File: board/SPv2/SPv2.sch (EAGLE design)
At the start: 64 parts, among them IC1 S34ML0XG1, IC2 F55[0/1]X---PT48, IC3 S34ML0XG1, IC4 74LS14D, IC5 F55[0/1]X---PT48, IC6 74LS14D, Q1 12MHz, Q2 12MHz

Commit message: Snap Pad v2, halfsies design, routed
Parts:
- removed C10, C9: 220nF, Passives:C0805
- removed C11, C12: 10pF, Passives:C0805
- removed C13, C15: 20pF, Passives:C0805
- removed C16: 470nF, Passives:C0805
- removed C8: 4.7uF, Passives:C0805
- removed D2: (no value), Passives:D-SCHOTTKY
- removed IC3: S34ML0XG1, Flash:S34ML0XG1
- removed IC5: F55[0/1]X---PT48, TI_MSP430_v16:F55[0/1]X---PT48
- removed IC6: 74LS14D, 74xx-us:74LS14D
- removed JP2: USBPCB, SparkFun-Connectors:USBPCB
- removed Q2: 12MHz, Passives:CRYSTALCSM-3X
- removed R10, R13: 1M, Passives:R0805
- removed R11: 1.4K 1%, Passives:R0805
- removed R12: 100 5%, Passives:R0805
- removed R14, R15: 1.4k, Passives:R0805
- removed R8, R9: 27 5%, Passives:R0805
- removed SJ2: (no value), jumper:SJW
- removed U$12, U$13, U$14, U$3: LED, Passives:LED
- removed U$15, U$16, U$17, U$18: 130, Passives:R0805
- IC2: value F55[0/1]X---PT48 -> F5508
- U$2: value FSMSM -> SNAP-HALF; device Passives:FSMSM -> Passives:SNAP-HALF
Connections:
- removed net !CE!_B: IC3.!CE, IC5.32
- removed net !RE!_B: IC3.!RE, IC5.35
- removed net !RST_B!: IC5.48, R13.1
- removed net !WE!_B: IC3.!WE, IC5.30
- removed net !WP!_B: IC3.!WP, IC5.29
- removed net +1V8_B: C10.1, IC5.43
- removed net +3V3_B: C9.1, IC3.VCC, IC5.11, IC5.28, IC5.42, IC5.7, R12.2, R13.2, U$12.ANODE, U$13.ANODE, U$14.ANODE, U$3.ANODE
- removed net ALE_B: IC3.ALE, IC5.22
- removed net CLE_B: IC3.CLE, IC5.31
- removed net D+_B: C11.1, IC5.38, R10.2, R11.1, R8.1
- removed net D-_B: C12.1, IC5.40, R9.1
- removed net DOUT_B: IC5.1, R14.1, R15.2
- removed net INTER_RXA_TXB: IC2.34, IC5.33
- removed net INTER_RXB_TXA: IC2.33, IC5.34
- removed net N$12: JP2.D+, R8.2
- removed net N$13: JP2.D-, R9.2
- removed net N$14: C16.1, IC5.13
- removed net N$15: U$13.CATHODE, U$17.1
- removed net N$16: U$12.CATHODE, U$16.1
- removed net N$17: U$15.1, U$3.CATHODE
- removed net N$18: U$14.CATHODE, U$18.1
- removed net N$20: IC5.9, U$18.2
- removed net N$21: IC5.8, U$17.2
- removed net N$29: IC5.6, U$16.2
- removed net N$30: IC5.5, U$15.2
- removed net N$31: R12.1, SJ2.2
- removed net N$34: IC6A.O, IC6B.I
- removed net N$35: IC6B.O, IC6C.I
- removed net N$36: IC6C.O, IC6D.I
- removed net N$37: IC6D.O, IC6E.I
- removed net N$38: IC6A.I, IC6E.O, IC6F.I
- removed net N$39: IC6F.O, R14.2
- removed net N$40: D2.ANODE, JP2.VBUS
- removed net NANDIO_A10: IC3.I/O2, IC5.16
- removed net NANDIO_A11: IC3.I/O3, IC5.17
- removed net NANDIO_A12: IC3.I/O4, IC5.18
- removed net NANDIO_A13: IC3.I/O5, IC5.19
- removed net NANDIO_A14: IC3.I/O6, IC5.20
- removed net NANDIO_A15: IC3.I/O7, IC5.21
- removed net NANDIO_A8: IC3.I/O0, IC5.14
- removed net NANDIO_A9: IC3.I/O1, IC5.15
- removed net PUR_B: IC5.39, R11.2, SJ2.1
- removed net R/B_B: IC3.R/!B, IC5.36
- removed net SW_B: IC5.4, U$2.B
- removed net TCK_B: IC5.26
- removed net TDI_B: IC5.24
- removed net TDO_B: IC5.23
- removed net TMS_B: IC5.25
- removed net TST_B: IC5.47
- removed net XT2IN_B: C13.2, IC5.45, Q2.1
- removed net XT2OUT_B: C15.2, IC5.46, Q2.2
- new net RX_A: IC2.34, U$2.RX
- new net TX_A: IC2.33, U$2.TX
- net GND: now also U$2.GND; no longer C10.2, C11.2, C12.2, C13.1, C15.1, C16.2, C8.2, C9.2, IC3.VSS, IC5.10, IC5.12, IC5.27, IC5.37, IC5.44, IC6P.GND, JP2.GND, R10.1, R15.1, U$2.A1
- net VBUS: now also U$2.V1, U$2.V2; no longer C8.1, D2.CATHODE, IC5.41, IC6P.VCC

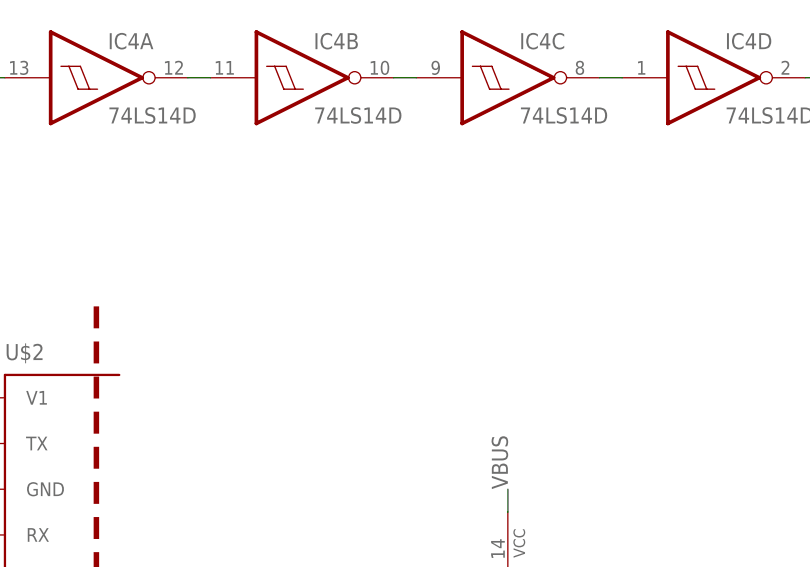
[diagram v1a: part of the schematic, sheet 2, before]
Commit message: added fiducals
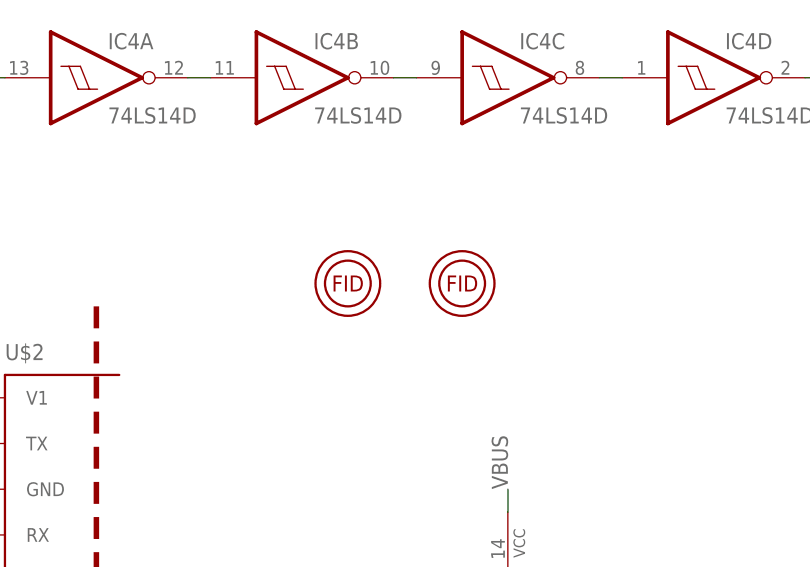
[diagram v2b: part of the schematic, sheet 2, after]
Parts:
- added U$12, U$3: FIDUCAL, Passives:FIDUCAL
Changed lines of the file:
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@@
 <part name="SUPPLY14" library="supply2" deviceset="GND" device=""/>
 <part name="U$2" library="Passives" deviceset="SNAP-HALF" device=""/>
+<part name="U$3" library="Passives" deviceset="FIDUCAL" device=""/>
+<part name="U$12" library="Passives" deviceset="FIDUCAL" device=""/>
 </parts>
 <sheets>
@@
 <instance part="SUPPLY13" gate="GND" x="71.12" y="17.78"/>
 <instance part="U$2" gate="G$1" x="-35.56" y="38.1"/>
+<instance part="U$3" gate="G$1" x="-7.62" y="60.96"/>
+<instance part="U$12" gate="G$1" x="5.08" y="60.96"/>
 </instances>
 <busses>
